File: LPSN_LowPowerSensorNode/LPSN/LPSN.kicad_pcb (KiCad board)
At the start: 2 copper layers, 33.3 x 29.2 mm, 12 parts, among them U2 SHT4x, U3 LPS22HB, U5 STM32U031F6Px, Y1 LSC

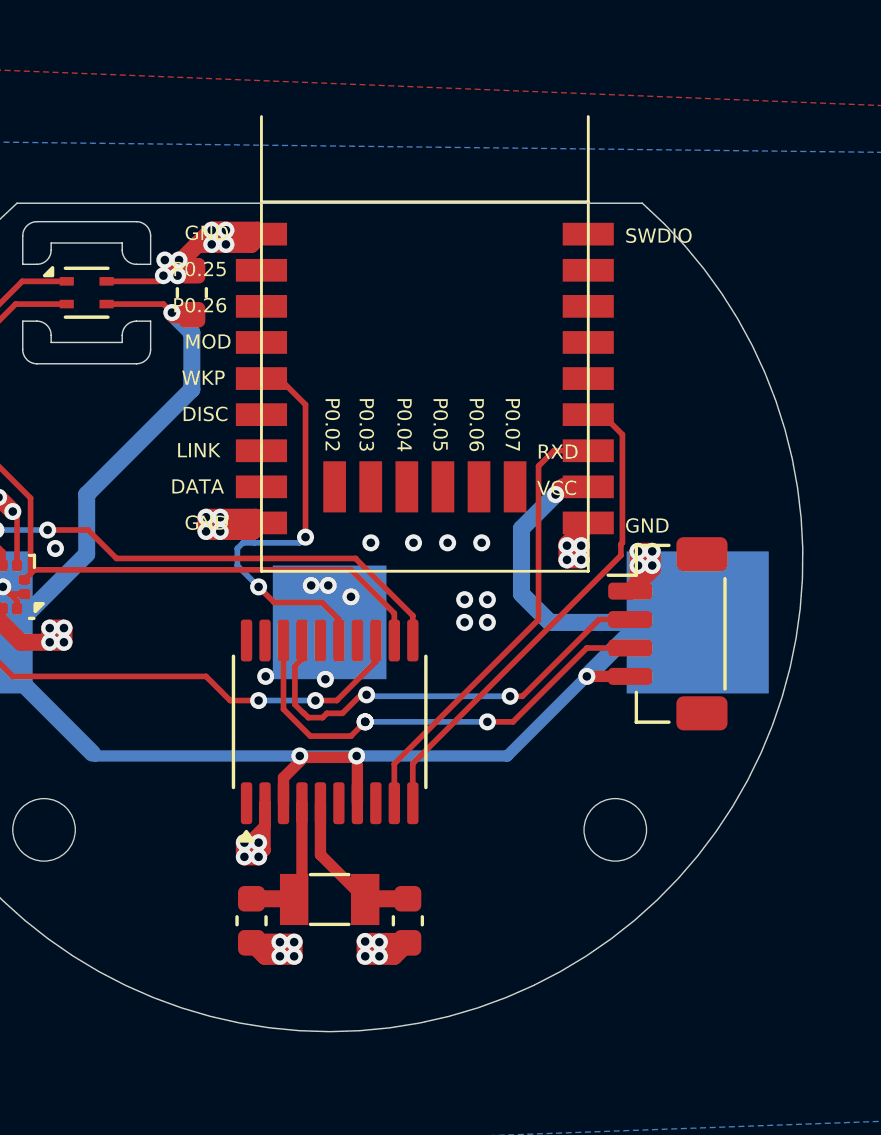
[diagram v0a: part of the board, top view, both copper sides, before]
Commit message: Ebyte correct footprint
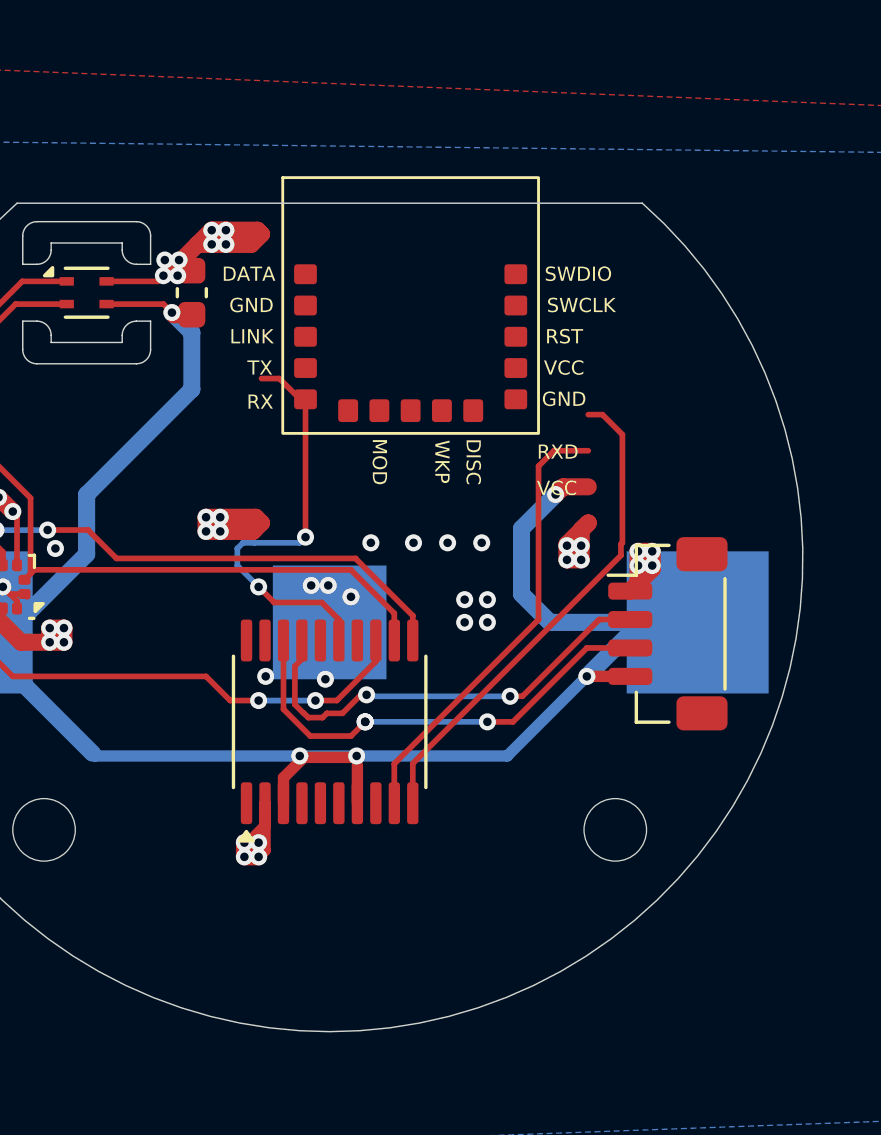
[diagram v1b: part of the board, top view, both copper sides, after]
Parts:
- removed C1, C2: 6p, Capacitor_SMD:C_0603_1608Metric
- removed U4: ~, Custom_foot:E104-BT5011A
- removed Y1: LSC, Crystal:Crystal_SMD_3215-2Pin_3.2x1.5mm
- added REF**: E104, EBYTE:Untitled, F.Cu at (145.9, 96.8)
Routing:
- net GND: track 55.3 -> 46.2 mm, vias 56 -> 48
- net LSC_N: track 5.55 -> 0.00 mm
- net LSC_P: track 5.01 -> 0.00 mm

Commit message: LPSN - backup
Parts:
- removed the ? at (153.8, 109.8)
- removed the ? at (133.7, 109.8)
- removed C3: 100n, Capacitor_SMD:C_0603_1608Metric
- removed STM_DB: JST_SH_BM04B-SRSS-TB_1x04-1MP_P1.00mm_Vertical, Connector_JST:JST_SH_BM04B-SRSS-TB_1x04-1MP_P1.00mm_Vertical
- added ?: , , F.Cu at (174.1, 119.5)
- added ?: , , F.Cu at (201.1, 119.5)
- added REF**: C_0603_1608Metric, Capacitor_SMD:C_0603_1608Metric, F.Cu at (192.9, 99.8)
- added REF**: R_0603_1608Metric, Resistor_SMD:R_0603_1608Metric, F.Cu at (158.1, 110.3)
- added REF**: C_0603_1608Metric, Capacitor_SMD:C_0603_1608Metric, F.Cu at (158.1, 101.9)
- added REF**: C_0805_2012Metric, Capacitor_SMD:C_0805_2012Metric, F.Cu at (155.6, 102.0)
- added REF**: C_0603_1608Metric, Capacitor_SMD:C_0603_1608Metric, F.Cu at (176.3, 96.1)
- added REF**: PinHeader_1x04_P2.54mm_Vertical, Connector_PinHeader_2.54mm:PinHeader_1x04_P2.54mm_Vertical, F.Cu at (200.6, 108.8)
- added REF**: PinHeader_1x02_P2.54mm_Vertical, Connector_PinHeader_2.54mm:PinHeader_1x02_P2.54mm_Vertical, F.Cu at (200.2, 96.4)
- added REF**: R_0805_2012Metric, Resistor_SMD:R_0805_2012Metric, F.Cu at (155.7, 110.5)
- added REF**: C_0805_2012Metric_Pad1.18x1.45mm_HandSolder, Capacitor_SMD:C_0805_2012Metric_Pad1.18x1.45mm_HandSolder, F.Cu at (194.7, 100.1)
- moved U5 45.3 mm to (187.8, 116.5), turned to -90 degrees
- moved BT1 45.3 mm to (187.7, 113.4), turned to 0 degrees
- moved U3 44.1 mm to (176.2, 105.3)
- moved U2 42.0 mm to (176.3, 99.6), turned to 90 degrees
- moved REF** 41.7 mm to (187.6, 96.8)
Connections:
- REF** pad 11: (no net) -> LPUART_TX
- REF** pad 12: (no net) -> LPUART_RX
- REF** pad 14: (no net) -> GND
- REF** pad 4: (no net) -> VCC
- REF** pad 5: (no net) -> GND
- REF** pad 7: (no net) -> GPIO_WAKEUP
- U5 pad 6: unconnected-(U5-PF2-Pad6) -> GPIO_WAKEUP
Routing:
- net VCC: track 76.2 -> 29.3 mm, vias 10 -> 0
- net GND: track 46.2 -> 0.00 mm, vias 48 -> 0
- net (no net): track 0.00 -> 16.9 mm
- net I2C_SDA: track 29.3 -> 24.2 mm, vias 3 -> 0
- net SW_CLK: track 15.8 -> 20.5 mm, vias 2 -> 0
- net PRESS_INT_READY: track 18.0 -> 21.6 mm, vias 2 -> 0
- net LPUART_TX: track 15.9 -> 14.5 mm
- net SW_DIO: track 16.3 -> 17.7 mm, vias 3 -> 0
- net I2C_SCL: track 26.9 -> 25.6 mm, vias 0 -> 2
- net LPUART_RX: track 17.5 -> 16.3 mm
- net GPIO_WAKEUP: track 14.9 -> 13.6 mm, vias 2 -> 0
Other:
- board size 33.3 x 29.2 mm -> 32 x 32 mm
- board text added: "Capacitors"
- board text added: "Resistors"
- board text removed: "RXD"
- board text removed: "VCC"

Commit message: LPSN - finalization of pcb
PCB almost done. Needs review and double checking
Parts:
- removed the REF** at (158.1, 101.9)
- removed the REF** at (155.6, 102.0)
- removed the REF** at (200.6, 108.8)
- removed the REF** at (200.2, 96.4)
- removed the REF** at (155.7, 110.5)
- added REF**: SolderJumper-3_P1.3mm_Bridged12_RoundedPad1.0x1.5mm, Jumper:SolderJumper-3_P1.3mm_Bridged12_RoundedPad1.0x1.5mm, F.Cu at (187.3, 104.4)
- added REF**: C_0603_1608Metric, Capacitor_SMD:C_0603_1608Metric, F.Cu at (177.0, 107.9)
- added REF**: C_0603_1608Metric, Capacitor_SMD:C_0603_1608Metric, F.Cu at (189.4, 111.1)
- added REF**: C_0603_1608Metric, Capacitor_SMD:C_0603_1608Metric, F.Cu at (192.6, 115.6)
- added REF**: C_0603_1608Metric, Capacitor_SMD:C_0603_1608Metric, F.Cu at (193.8, 96.1)
- added REF**: PinHeader_1x05_P2.54mm_Vertical, Connector_PinHeader_2.54mm:PinHeader_1x05_P2.54mm_Vertical, F.Cu at (200.6, 108.8)
- added REF**: C_0603_1608Metric, Capacitor_SMD:C_0603_1608Metric, F.Cu at (186.8, 111.1)
- added REF**: C_0805_2012Metric_Pad1.18x1.45mm_HandSolder, Capacitor_SMD:C_0805_2012Metric_Pad1.18x1.45mm_HandSolder, F.Cu at (191.9, 111.6)
- moved REF** 37.9 mm to (193.8, 97.6), turned to 0 degrees
- moved REF** 1.11 mm to (177.4, 96.2)
- moved U2 1.11 mm to (177.4, 99.7)
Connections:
- BT1 pad 2: GND -> (no net)
- REF** pad 2: GND -> (no net) (x3)
- REF** pad 2: GND -> VCC
- REF** pad 14: GND -> (no net)
- REF** pad 3: (no net) -> VCC
- REF** pad 5: GND -> (no net)
- U2 pad 4: GND -> (no net)
- U3 pad 3: GND -> (no net)
- U3 pad 5: GND -> (no net)
- U3 pad 8: GND -> (no net)
- U3 pad 9: GND -> (no net)
- U5 pad 14: unconnected-(U5-PA8/PA9/PA10-Pad14) -> (no net)
- U5 pad 2: GND -> (no net)
- U5 pad 20: unconnected-(U5-PF3-Pad20) -> (no net)
- U5 pad 4: LSC_P -> (no net)
- U5 pad 5: LSC_N -> (no net)
- U5 pad 6: GPIO_WAKEUP -> (no net)
- U5 pad 8: unconnected-(U5-PA0-Pad8) -> GPIO_WAKEUP
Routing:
- net VCC: track 29.3 -> 128.8 mm, vias 0 -> 4
- net (no net): track 16.9 -> 81.2 mm, vias 0 -> 4
- net GND: track 0.00 -> 26.3 mm, vias 0 -> 21
- net SW_CLK: track 20.5 -> 22.5 mm
- net SW_DIO: track 17.7 -> 19.6 mm
- net GPIO_WAKEUP: track 13.6 -> 15.5 mm
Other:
- outline, holes or cut-outs redrawn
- board text removed: "Capacitors"
- board text removed: "Resistors"

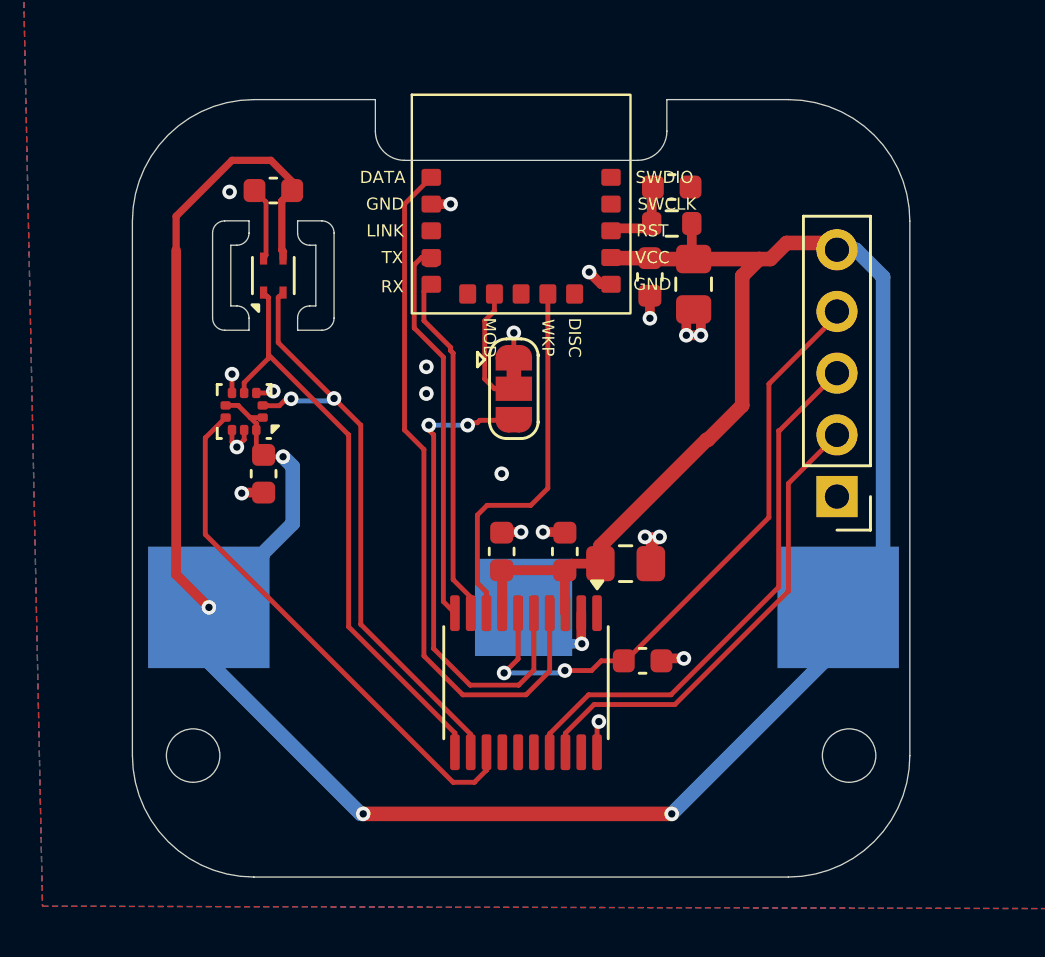
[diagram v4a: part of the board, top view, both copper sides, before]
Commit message: LPSN - production with gerber files v0.1
Version that was send to JLCPCB
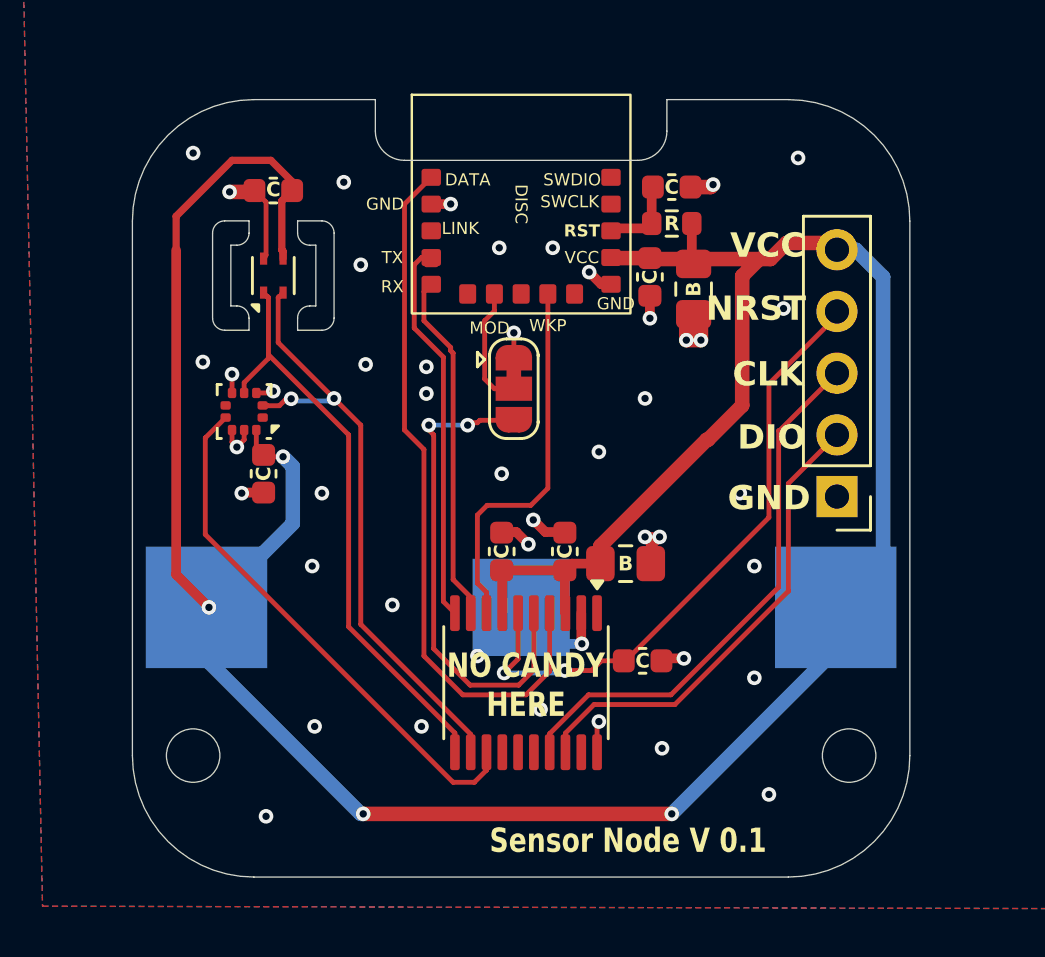
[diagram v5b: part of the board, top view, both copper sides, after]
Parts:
- moved REF** 0.20 mm to (194.7, 100.3)
- moved BT1 0.10 mm to (187.6, 113.4)
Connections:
- BT1 pad 2: (no net) -> GND
- REF** pad 2: (no net) -> GND (x7)
- REF** pad 14: (no net) -> GND
- REF** pad 5: (no net) -> GND
- U2 pad 4: (no net) -> GND
- U5 pad 15: GPIO_WAKEUP -> (no net)
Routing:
- net GND: track 26.3 -> 30.3 mm, vias 21 -> 46
- net VCC: track 128.8 -> 126.5 mm
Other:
- board text added: "B"
- board text added: "C"
- board text added: "CLK"
- board text added: "DIO"
- board text added: "GND"
- board text added: "NO CANDY HERE"
- board text added: "NRST"
- board text added: "R"
- board text added: "Sensor Node V 0.1"
- board text added: "VCC"
